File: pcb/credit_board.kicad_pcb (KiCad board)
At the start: 2 copper layers, 11 parts, among them J1 Conn_01x05_Male, J2 Conn_01x03_Male, J3 Jack-DC, U1 74HC04, Y1 10MHz, Y2 32.768 kHz

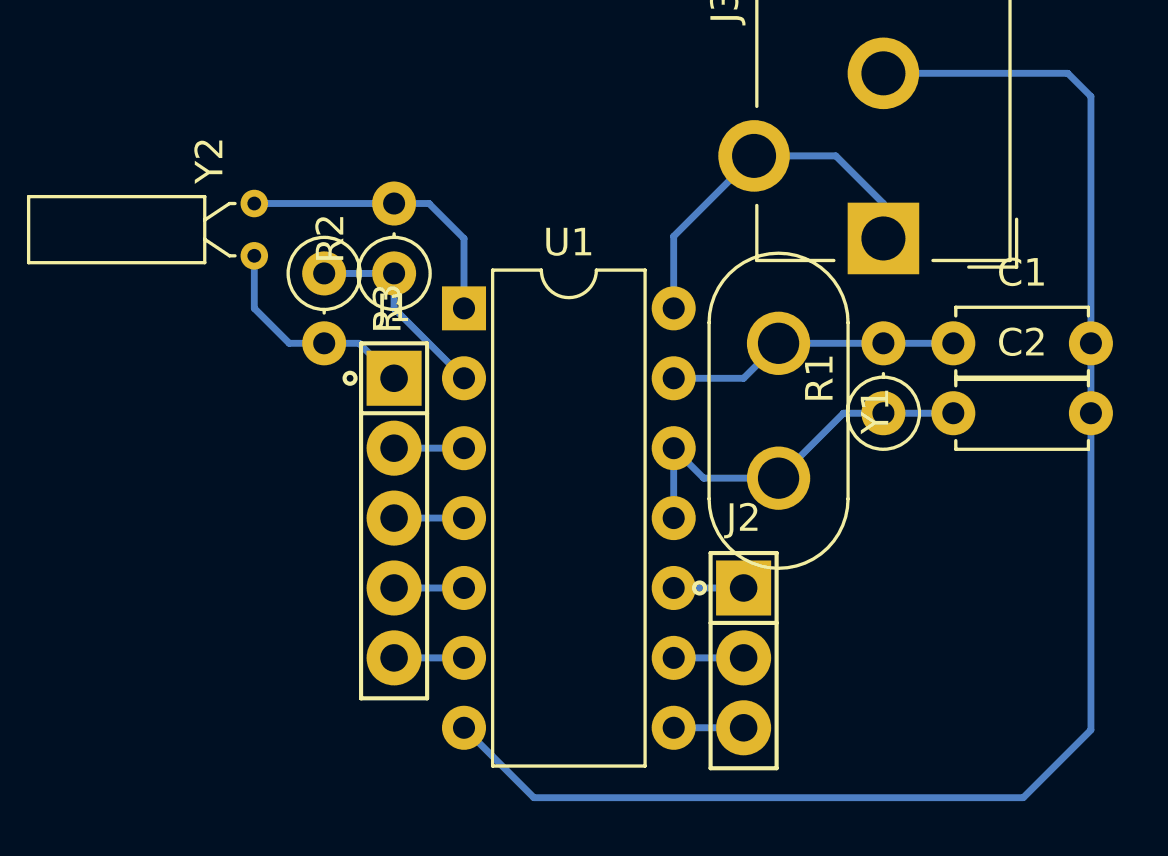
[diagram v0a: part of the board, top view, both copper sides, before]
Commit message: no connected pins are pull up by 10k resistors.
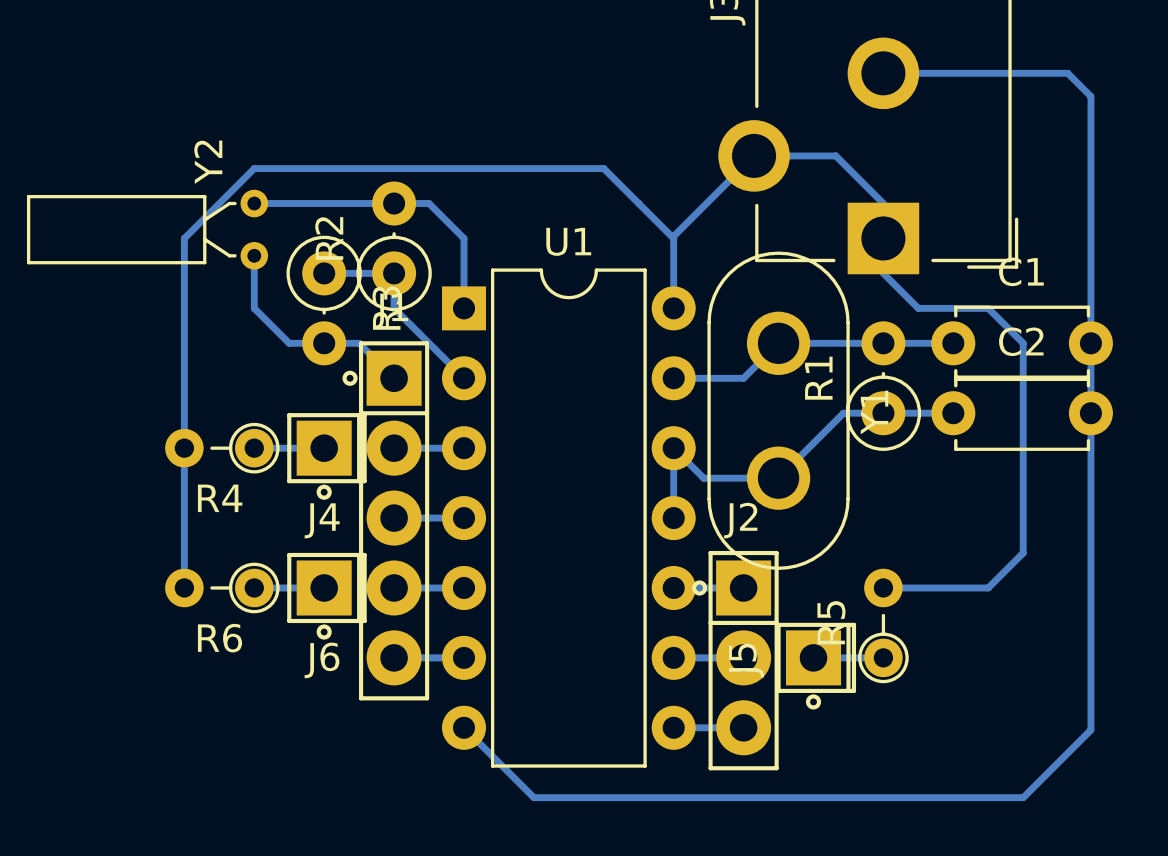
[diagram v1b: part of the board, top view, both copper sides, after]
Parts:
- added J4: pull-up, PINHEADER:PINHEADER_1x1, F.Cu at (148.6, 119.4)
- added J5: pull-up, PINHEADER:PINHEADER_1x1, F.Cu at (166.4, 127.0)
- added J6: pull-up, PINHEADER:PINHEADER_1x1, F.Cu at (148.6, 124.5)
- added R4: 10k, Resistors_THT:R_Axial_DIN0204_L3.6mm_D1.6mm_P2.54mm_Vertical, F.Cu at (146.1, 119.4)
- added R5: 10k, Resistors_THT:R_Axial_DIN0204_L3.6mm_D1.6mm_P2.54mm_Vertical, F.Cu at (168.9, 127.0)
- added R6: 10k, Resistors_THT:R_Axial_DIN0204_L3.6mm_D1.6mm_P2.54mm_Vertical, F.Cu at (146.1, 124.5)
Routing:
- net VCC: track 13.4 -> 66.6 mm
- net Net-(J6-Pad1): track 0.00 -> 2.54 mm
- net Net-(J5-Pad1): track 0.00 -> 2.54 mm
- net Net-(J4-Pad1): track 0.00 -> 2.54 mm

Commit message: completed to make a initial credit board.
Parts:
- J1: value Conn_01x05_Male -> amp or pull-up; footprint PINHEADER:PINHEADER_1x5 -> PINHEADER:PINHEADER_1x3
- J2: value Conn_01x03_Male -> amp or pull-up
- J4: value pull-up -> amp or pull-up; footprint PINHEADER:PINHEADER_1x1 -> PINHEADER:PINHEADER_1x3
- J5, J6: value pull-up -> clk
- Y2: footprint Crystals:Crystal_DS26_d2.0mm_l6.0mm_Horizontal -> Crystals:Crystal_AT310_d3.0mm_l10.0mm_Vertical
- moved J3 8.98 mm to (162.6, 105.4), turned to 90 degrees
- moved Y2 6.35 mm to (152.4, 110.5), turned to 180 degrees
- moved J6 5.39 mm to (152.4, 128.3)
- moved J5 5.39 mm to (162.6, 130.8)
- moved J1 4.02 mm to (147.3, 115.6)
- moved J4 4.02 mm to (152.4, 120.7), turned to 0 degrees
- moved R6 4.02 mm to (149.9, 125.7)
- moved R1 2.84 mm to (167.6, 120.7)
- moved C2 2.84 mm to (170.2, 120.7)
- moved R2 2.84 mm to (152.4, 115.6)
- moved R3 2.84 mm to (149.9, 115.6), turned to 90 degrees
- moved R4 1.80 mm to (144.8, 120.7)
- moved R5 1.80 mm to (167.6, 128.3), turned to 0 degrees
- moved U1 1.80 mm to (154.9, 113.0)
- moved J2 1.80 mm to (165.1, 123.2)
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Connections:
- R4 pad 1: Net-(J4-Pad1) -> Net-(J1-Pad3)
- R5 pad 1: Net-(J5-Pad1) -> Net-(J2-Pad3)
- R6 pad 1: Net-(J6-Pad1) -> Net-(J4-Pad3)
- U1 pad 4: Net-(J1-Pad3) -> Net-(J4-Pad1)
- U1 pad 5: Net-(J1-Pad4) -> Net-(J4-Pad2)
- U1 pad 6: Net-(J1-Pad5) -> Net-(J6-Pad1)
- U1 pad 8: Net-(J2-Pad3) -> Net-(J5-Pad1)
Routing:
- net VCC: track 66.6 -> 76.2 mm
- net Net-(R2-Pad2): track 10.7 -> 5.08 mm
- net Net-(J1-Pad2): track 3.30 -> 7.62 mm
- net Net-(C2-Pad1): track 14.1 -> 10.2 mm
- net Net-(J1-Pad4): track 3.30 -> 0.00 mm
- net Net-(J4-Pad3): track 0.00 -> 2.54 mm
- net Net-(J4-Pad2): track 0.00 -> 2.54 mm
- net Net-(J1-Pad5): track 2.54 -> 0.00 mm
- net Net-(R2-Pad1): track 7.40 -> 5.08 mm
- net Net-(J1-Pad1): track 8.04 -> 6.13 mm
- net GND: track 55.8 -> 54.7 mm, vias 0 -> 2
- net Net-(J6-Pad1): track 2.54 -> 3.59 mm
- net Net-(C1-Pad1): track 10.7 -> 9.72 mm
- net Net-(J2-Pad2): track 3.30 -> 2.54 mm

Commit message: 細かな修正。これで本当に完成。
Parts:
- moved R4 3.59 mm to (147.3, 123.2), turned to 270 degrees
- moved R5 3.59 mm to (165.1, 130.8), turned to 270 degrees
- turned R6 to 270 degrees
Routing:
- net VCC: track 76.2 -> 61.1 mm
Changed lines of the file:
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@@
     (links 31)
     (no_connects 0)
-    (area 0 0 0 0)
+    (area 141.004999 98.684999 176.985001 136.690002)
     (thickness 1.6)
     (drawings 0)
-    (tracks 52)
+    (tracks 51)
     (zones 0)
     (modules 17)
@@
     (add_net VCC)
   )
+  (module Resistors_THT:R_Axial_DIN0204_L3.6mm_D1.6mm_P2.54mm_Vertical (layer F.Cu)
+    (at 165.1 130.81 270)
+    (descr "Resistor, Axial_DIN0204 series, Axial, Vertical, pin pitch=2.54mm, 0.16666666666666666W = 1/6W, length*diameter=3.6*1.6mm^2, http://cdn-reichelt.de/documents/datenblatt/B400/1_4W%23YAG.pdf")
+    (tags "Resistor Axial_DIN0204 series Axial Vertical pin pitch 2.54mm 0.16666666666666666W = 1/6W length 3.6mm diameter 1.6mm")
+    (fp_text reference R5 (at 1.27 -1.86 270) (layer F.SilkS)
+      (effects (font (size 1 1) (thickness 0.15)))
+    )
+    (fp_text value 10k (at 1.27 1.86 270) (layer F.Fab)
+      (effects (font (size 1 1) (thickness 0.15)))
+    )
+    (fp_circle (center 0 0) (end 0.8 0) (layer F.Fab) (width 0.1))
+    (fp_circle (center 0 0) (end 0.86 0) (layer F.SilkS) (width 0.12))
+    (fp_line (start 0 0) (end 2.54 0) (layer F.Fab) (width 0.1))
+    (fp_line (start 0.86 0) (end 1.54 0) (layer F.SilkS) (width 0.12))
+    (fp_line (start -1.15 -1.15) (end -1.15 1.15) (layer F.CrtYd) (width 0.05))
+    (fp_line (start -1.15 1.15) (end 3.55 1.15) (layer F.CrtYd) (width 0.05))
+    (fp_line (start 3.55 1.15) (end 3.55 -1.15) (layer F.CrtYd) (width 0.05))
+    (fp_line (start 3.55 -1.15) (end -1.15 -1.15) (layer F.CrtYd) (width 0.05))
+    (pad 1 thru_hole circle (at 0 0 270) (size 1.4 1.4) (drill 0.7) (layers *.Cu *.Mask)
+      (net 9 "Net-(J2-Pad3)"))
+    (pad 2 thru_hole oval (at 2.54 0 270) (size 1.4 1.4) (drill 0.7) (layers *.Cu *.Mask)
+      (net 12 VCC))
+    (model ${KISYS3DMOD}/Resistors_THT.3dshapes/R_Axial_DIN0204_L3.6mm_D1.6mm_P2.54mm_Vertical.wrl
+      (at (xyz 0 0 0))
+      (scale (xyz 0.393701 0.393701 0.393701))
+      (rotate (xyz 0 0 0))
+    )
+  )
   (module Crystals:Crystal_HC50_Vertical (layer F.Cu)
     (at 165.1 115.75 270)
@@
   )
   (module Resistors_THT:R_Axial_DIN0204_L3.6mm_D1.6mm_P2.54mm_Vertical (layer F.Cu)
-    (at 144.78 120.65 180)
+    (at 147.32 123.19 270)
     (descr "Resistor, Axial_DIN0204 series, Axial, Vertical, pin pitch=2.54mm, 0.16666666666666666W = 1/6W, length*diameter=3.6*1.6mm^2, http://cdn-reichelt.de/documents/datenblatt/B400/1_4W%23YAG.pdf")
     (tags "Resistor Axial_DIN0204 series Axial Vertical pin pitch 2.54mm 0.16666666666666666W = 1/6W length 3.6mm diameter 1.6mm")
-    (fp_text reference R4 (at 1.27 -1.86 180) (layer F.SilkS)
-      (effects (font (size 1 1) (thickness 0.15)))
-    )
-    (fp_text value 10k (at 1.27 1.86 180) (layer F.Fab)
+    (fp_text reference R4 (at 1.27 -1.86 270) (layer F.SilkS)
+      (effects (font (size 1 1) (thickness 0.15)))
+    )
+    (fp_text value 10k (at 1.27 1.86 270) (layer F.Fab)
       (effects (font (size 1 1) (thickness 0.15)))
     )
@@
     (fp_line (start 3.55 1.15) (end 3.55 -1.15) (layer F.CrtYd) (width 0.05))
     (fp_line (start 3.55 -1.15) (end -1.15 -1.15) (layer F.CrtYd) (width 0.05))
-    (pad 1 thru_hole circle (at 0 0 180) (size 1.4 1.4) (drill 0.7) (layers *.Cu *.Mask)
+    (pad 1 thru_hole circle (at 0 0 270) (size 1.4 1.4) (drill 0.7) (layers *.Cu *.Mask)
       (net 6 "Net-(J1-Pad3)"))
-    (pad 2 thru_hole oval (at 2.54 0 180) (size 1.4 1.4) (drill 0.7) (layers *.Cu *.Mask)
+    (pad 2 thru_hole oval (at 2.54 0 270) (size 1.4 1.4) (drill 0.7) (layers *.Cu *.Mask)
       (net 12 VCC))
     (model ${KISYS3DMOD}/Resistors_THT.3dshapes/R_Axial_DIN0204_L3.6mm_D1.6mm_P2.54mm_Vertical.wrl
@@
   )
   (module Resistors_THT:R_Axial_DIN0204_L3.6mm_D1.6mm_P2.54mm_Vertical (layer F.Cu)
-    (at 167.64 128.27)
+    (at 149.86 125.73 270)
     (descr "Resistor, Axial_DIN0204 series, Axial, Vertical, pin pitch=2.54mm, 0.16666666666666666W = 1/6W, length*diameter=3.6*1.6mm^2, http://cdn-reichelt.de/documents/datenblatt/B400/1_4W%23YAG.pdf")
     (tags "Resistor Axial_DIN0204 series Axial Vertical pin pitch 2.54mm 0.16666666666666666W = 1/6W length 3.6mm diameter 1.6mm")
-    (fp_text reference R5 (at 1.27 -1.86) (layer F.SilkS)
-      (effects (font (size 1 1) (thickness 0.15)))
-    )
-    (fp_text value 10k (at 1.27 1.86) (layer F.Fab)
+    (fp_text reference R6 (at 1.27 -1.86 270) (layer F.SilkS)
+      (effects (font (size 1 1) (thickness 0.15)))
+    )
+    (fp_text value 10k (at 1.27 1.86 270) (layer F.Fab)
       (effects (font (size 1 1) (thickness 0.15)))
     )
@@
     (fp_line (start 3.55 1.15) (end 3.55 -1.15) (layer F.CrtYd) (width 0.05))
     (fp_line (start 3.55 -1.15) (end -1.15 -1.15) (layer F.CrtYd) (width 0.05))
-    (pad 1 thru_hole circle (at 0 0) (size 1.4 1.4) (drill 0.7) (layers *.Cu *.Mask)
-      (net 9 "Net-(J2-Pad3)"))
-    (pad 2 thru_hole oval (at 2.54 0) (size 1.4 1.4) (drill 0.7) (layers *.Cu *.Mask)
-      (net 12 VCC))
-    (model ${KISYS3DMOD}/Resistors_THT.3dshapes/R_Axial_DIN0204_L3.6mm_D1.6mm_P2.54mm_Vertical.wrl
-      (at (xyz 0 0 0))
-      (scale (xyz 0.393701 0.393701 0.393701))
-      (rotate (xyz 0 0 0))
-    )
-  )
-  (module Resistors_THT:R_Axial_DIN0204_L3.6mm_D1.6mm_P2.54mm_Vertical (layer F.Cu)
-    (at 149.86 125.73 180)
-    (descr "Resistor, Axial_DIN0204 series, Axial, Vertical, pin pitch=2.54mm, 0.16666666666666666W = 1/6W, length*diameter=3.6*1.6mm^2, http://cdn-reichelt.de/documents/datenblatt/B400/1_4W%23YAG.pdf")
-    (tags "Resistor Axial_DIN0204 series Axial Vertical pin pitch 2.54mm 0.16666666666666666W = 1/6W length 3.6mm diameter 1.6mm")
-    (fp_text reference R6 (at 1.27 -1.86 180) (layer F.SilkS)
-      (effects (font (size 1 1) (thickness 0.15)))
-    )
-    (fp_text value 10k (at 1.27 1.86 180) (layer F.Fab)
-      (effects (font (size 1 1) (thickness 0.15)))
-    )
-    (fp_circle (center 0 0) (end 0.8 0) (layer F.Fab) (width 0.1))
-    (fp_circle (center 0 0) (end 0.86 0) (layer F.SilkS) (width 0.12))
-    (fp_line (start 0 0) (end 2.54 0) (layer F.Fab) (width 0.1))
-    (fp_line (start 0.86 0) (end 1.54 0) (layer F.SilkS) (width 0.12))
-    (fp_line (start -1.15 -1.15) (end -1.15 1.15) (layer F.CrtYd) (width 0.05))
-    (fp_line (start -1.15 1.15) (end 3.55 1.15) (layer F.CrtYd) (width 0.05))
-    (fp_line (start 3.55 1.15) (end 3.55 -1.15) (layer F.CrtYd) (width 0.05))
-    (fp_line (start 3.55 -1.15) (end -1.15 -1.15) (layer F.CrtYd) (width 0.05))
-    (pad 1 thru_hole circle (at 0 0 180) (size 1.4 1.4) (drill 0.7) (layers *.Cu *.Mask)
+    (pad 1 thru_hole circle (at 0 0 270) (size 1.4 1.4) (drill 0.7) (layers *.Cu *.Mask)
       (net 17 "Net-(J4-Pad3)"))
-    (pad 2 thru_hole oval (at 2.54 0 180) (size 1.4 1.4) (drill 0.7) (layers *.Cu *.Mask)
+    (pad 2 thru_hole oval (at 2.54 0 270) (size 1.4 1.4) (drill 0.7) (layers *.Cu *.Mask)
       (net 12 VCC))
     (model ${KISYS3DMOD}/Resistors_THT.3dshapes/R_Axial_DIN0204_L3.6mm_D1.6mm_P2.54mm_Vertical.wrl
@@
   (segment (start 149.86 113.03) (end 147.32 115.57) (width 0.25) (layer B.Cu) (net 4))
   (segment (start 154.94 118.11) (end 147.32 118.11) (width 0.25) (layer B.Cu) (net 5))
-  (segment (start 147.32 120.65) (end 144.78 120.65) (width 0.25) (layer B.Cu) (net 6))
+  (segment (start 147.32 123.19) (end 147.32 120.65) (width 0.25) (layer B.Cu) (net 6))
   (segment (start 162.56 123.19) (end 165.1 123.19) (width 0.25) (layer B.Cu) (net 7))
   (segment (start 165.1 125.73) (end 162.56 125.73) (width 0.25) (layer B.Cu) (net 8))
-  (segment (start 165.1 128.27) (end 167.64 128.27) (width 0.25) (layer B.Cu) (net 9))
+  (segment (start 165.1 130.81) (end 165.1 128.27) (width 0.25) (layer B.Cu) (net 9))
   (segment (start 152.4 115.57) (end 154.94 115.57) (width 0.25) (layer B.Cu) (net 10))
   (segment (start 149.86 115.57) (end 152.4 115.57) (width 0.25) (layer B.Cu) (net 10))
   (segment (start 152.4 113.03) (end 152.4 110.49) (width 0.25) (layer B.Cu) (net 11))
   (segment (start 154.94 113.03) (end 152.4 113.03) (width 0.25) (layer B.Cu) (net 11))
-  (segment (start 160.02 133.35) (end 149.86 133.35) (width 0.25) (layer B.Cu) (net 12))
+  (segment (start 151.13 133.35) (end 160.02 133.35) (width 0.25) (layer B.Cu) (net 12))
+  (segment (start 149.86 132.08) (end 151.13 133.35) (width 0.25) (layer B.Cu) (net 12))
+  (segment (start 149.86 128.27) (end 149.86 132.08) (width 0.25) (layer B.Cu) (net 12))
+  (segment (start 149.86 128.27) (end 147.32 125.73) (width 0.25) (layer B.Cu) (net 12))
+  (segment (start 165.1 133.35) (end 160.02 133.35) (width 0.25) (layer B.Cu) (net 12))
   (segment (start 160.02 130.81) (end 160.02 115.57) (width 0.25) (layer B.Cu) (net 12))
   (segment (start 160.02 133.35) (end 160.02 130.81) (width 0.25) (layer B.Cu) (net 12))
   (segment (start 160.02 130.81) (end 160.02 128.27) (width 0.25) (layer B.Cu) (net 12))
-  (segment (start 170.18 128.27) (end 165.1 133.35) (width 0.25) (layer B.Cu) (net 12))
-  (segment (start 165.1 133.35) (end 160.02 133.35) (width 0.25) (layer B.Cu) (net 12))
   (segment (start 160.02 115.57) (end 162.56 113.03) (width 0.25) (layer B.Cu) (net 12))
   (segment (start 162.56 113.03) (end 162.56 105.41) (width 0.25) (layer B.Cu) (net 12))
-  (segment (start 147.32 130.81) (end 147.32 125.73) (width 0.25) (layer B.Cu) (net 12))
-  (segment (start 149.86 133.35) (end 147.32 130.81) (width 0.25) (layer B.Cu) (net 12))
   (segment (start 162.56 105.41) (end 162.56 102.87) (width 0.25) (layer B.Cu) (net 12))
   (segment (start 162.56 102.87) (end 163.4 102.87) (width 0.25) (layer B.Cu) (net 12))
   (segment (start 163.4 102.87) (end 165.56 100.71) (width 0.25) (layer B.Cu) (net 12))
-  (segment (start 142.24 120.65) (end 147.32 125.73) (width 0.25) (layer B.Cu) (net 12))
   (segment (start 152.4 120.65) (end 154.94 120.65) (width 0.25) (layer B.Cu) (net 13))
   (segment (start 162.56 130.81) (end 162.56 128.27) (width 0.25) (layer B.Cu) (net 14))

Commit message: 本当の，本当に完成したよぉぉぉぉ。
神経質には完成させられないんじゃないだろうか？と完成を危ぶんだこともありました。
しかし，なんとか完成しました。
めでたし。めでたし。
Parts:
- J1, J2, J4: footprint PINHEADER:PINHEADER_1x3 -> Pin_Headers:Pin_Header_Straight_1x03_Pitch2.54mm
- J5, J6: footprint PINHEADER:PINHEADER_1x1 -> Pin_Headers:Pin_Header_Straight_1x01_Pitch2.54mm
- R4, R5, R6: footprint Resistors_THT:R_Axial_DIN0204_L3.6mm_D1.6mm_P2.54mm_Vertical -> Resistors_THT:R_Axial_DIN0207_L6.3mm_D2.5mm_P2.54mm_Vertical
- moved J2 7.62 mm to (172.7, 123.2)
- moved R1 5.68 mm to (172.7, 118.1)
- moved R5 5.68 mm to (170.2, 128.3), turned to 180 degrees
- moved C1 5.08 mm to (175.3, 115.6)
- moved C2 5.08 mm to (175.3, 120.7)
- moved J6 3.59 mm to (154.9, 130.8)
- moved R4 3.59 mm to (144.8, 120.7), turned to 180 degrees
- moved Y1 2.54 mm to (167.6, 115.8)
- turned R6 to 180 degrees
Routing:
- net VCC: track 61.1 -> 73.6 mm
- net Net-(C2-Pad1): track 10.2 -> 18.9 mm
- net Net-(J2-Pad2): track 2.54 -> 10.2 mm
- net Net-(J2-Pad1): track 2.54 -> 10.2 mm
- net GND: track 54.7 -> 60.3 mm
- net Net-(J6-Pad1): track 3.59 -> 7.18 mm
- net Net-(C1-Pad1): track 9.72 -> 13.0 mm
- net Net-(J2-Pad3): track 2.54 -> 5.08 mm
